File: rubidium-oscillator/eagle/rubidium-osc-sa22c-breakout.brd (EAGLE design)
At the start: 49.8 x 56.6 mm, 13 parts, among them J1 OSC_TMMH-109-01-G-DV-ES-A, Q1 ZXMP10A13F, Q2 ZXMP10A13F, X1 MKDSN4, X2 MPT3, X3 MPT6, X4 SMA-142-0701-801/806, X5 SMA-142-0701-801/806, X6 SMA-142-0701-801/806

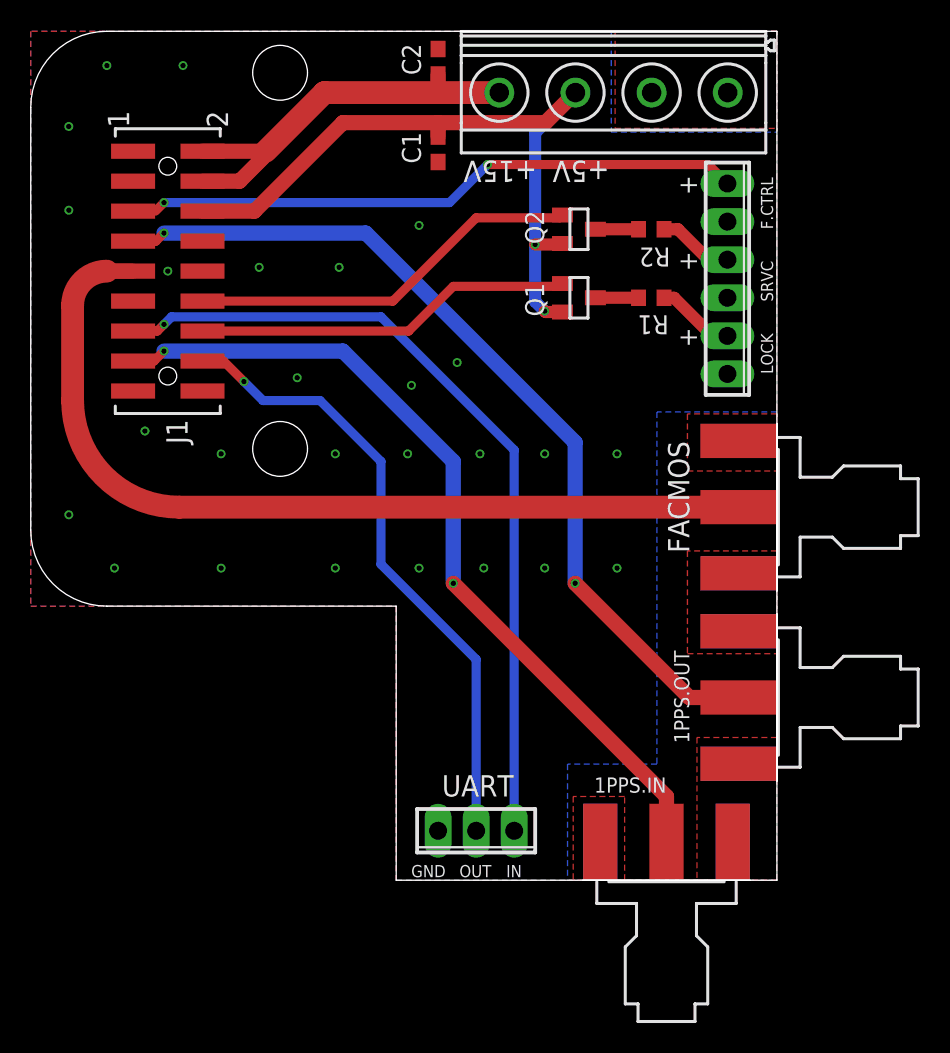
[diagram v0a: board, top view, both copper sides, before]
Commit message: Added thermals, moved SMAs, updated SMA gnds, fixed board corners, fixed gnd vias
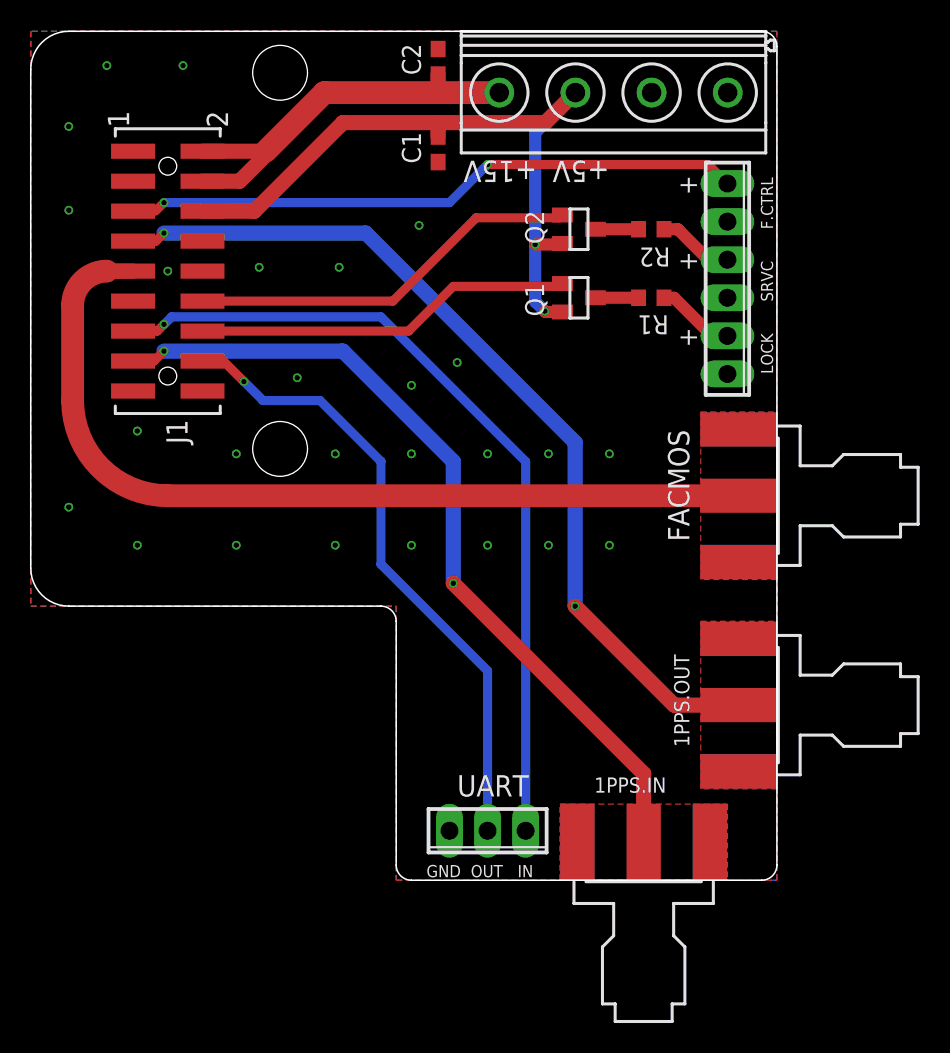
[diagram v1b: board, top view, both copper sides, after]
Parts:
- moved X6 1.52 mm to (40.9, -18.3)
- moved X2 0.76 mm to (30.5, -15.0)
- moved X4 0.76 mm to (49.8, 7.37)
- moved X5 0.51 mm to (49.8, -6.60)
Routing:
- net N$2: track 59.0 -> 60.1 mm
- net N$3: track 56.0 -> 55.3 mm
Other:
- outline, holes or cut-outs redrawn
